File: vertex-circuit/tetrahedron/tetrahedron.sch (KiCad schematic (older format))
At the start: 9 parts, among them J1 DIP-BLACK-MALE-HEADER-VERT_4P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, J2 DIP-BLACK-MALE-HEADER-VERT_4P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, J3 DIP-BLACK-MALE-HEADER-VERT_4P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, J4 DIP-BLACK-MALE-HEADER-VERT_4P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, J5 JACK-DC-005, J6 DIP-BLACK-MALE-HEADER-VERT_4P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, J7 DIP-BLACK-MALE-HEADER-VERT_4P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, J8 DIP-BLACK-MALE-HEADER-VERT_4P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

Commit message: save circuits
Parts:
- removed J2, J3, J7, J8: DIP-BLACK-MALE-HEADER-VERT_4P-2.54_, SeeedOPL-Connector-2016:H4-2.54, symbol DIP-BLACK-MALE-HEADER-VERT_4P-2.54_
- added J5: d, SeeedOPL-Connector-2016:H4-2.54, symbol DIP-BLACK-MALE-HEADER-VERT_4P-2.54_
- J1: renamed from J5; value JACK-DC-005 -> DC 5v
- J2: renamed from J6; value DIP-BLACK-MALE-HEADER-VERT_4P-2.54_ -> a
- J3: renamed from J1; value DIP-BLACK-MALE-HEADER-VERT_4P-2.54_ -> b
- J4: value DIP-BLACK-MALE-HEADER-VERT_4P-2.54_ -> c
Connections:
- net GND: now reaches J2.1 (P$1), J3.1 (P$1)
- net GND: now also C1.2, J1.-1 (-), J4.1 (P$1), J5.1 (P$1)
- net +5V: now reaches J2.4 (P$4), J3.4 (P$4)
- net +5V: now also C1.1, J1.+, J4.4 (P$4), J5.4 (P$4)
- net at J4.2 (P$2): now also J5.2 (P$2)
- net at J4.3 (P$3): now also J5.3 (P$3)
- no-connect marks 19 -> 1
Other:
- moved on the sheet: C1, J1, J2, J3, J4

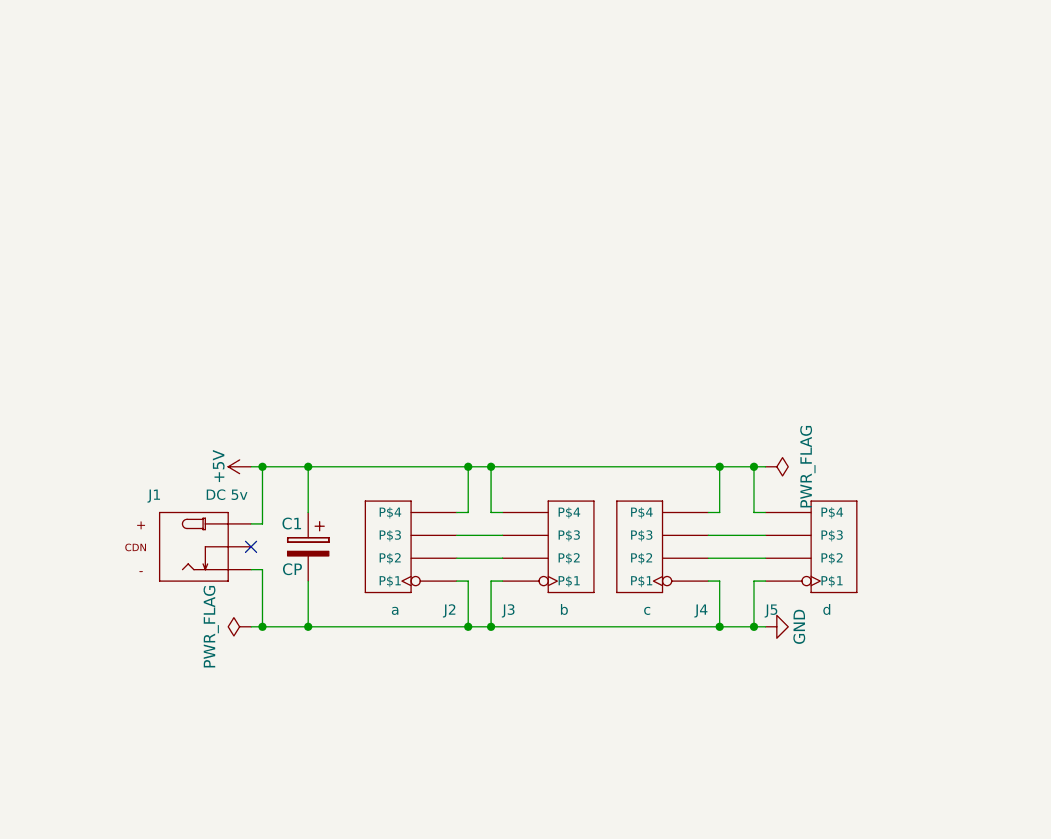
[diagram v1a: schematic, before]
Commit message: shematic electrical problems were only warnings! move on to pcb
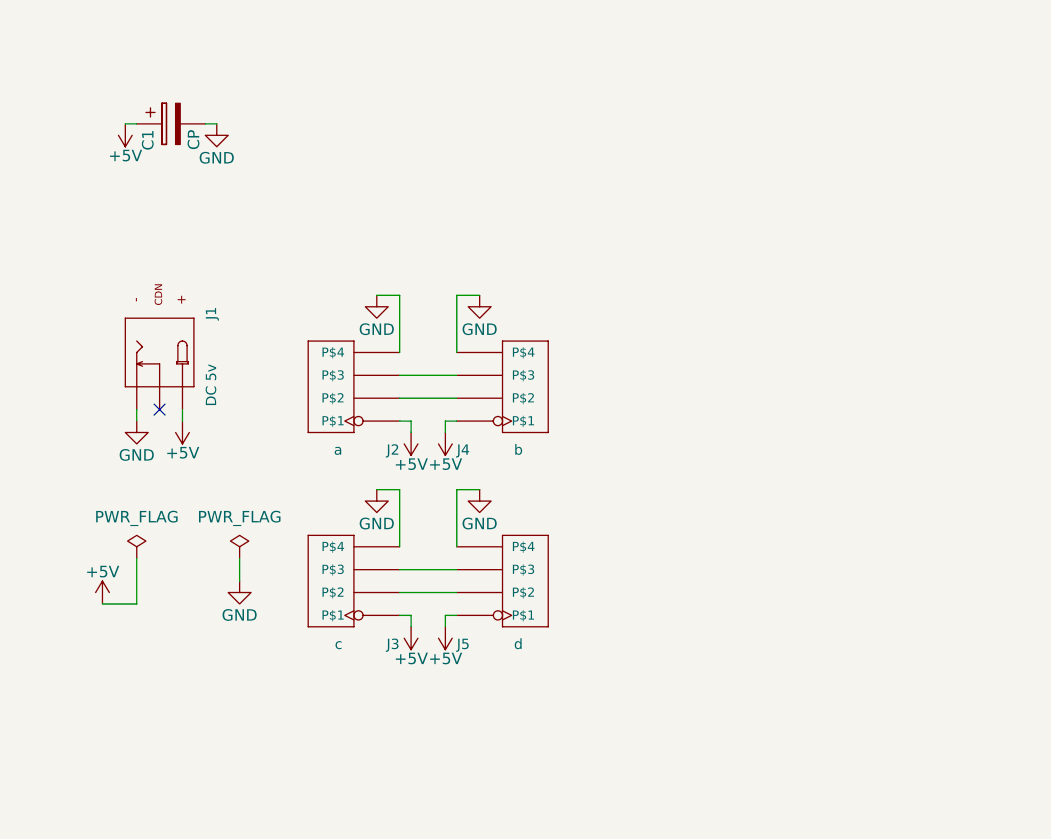
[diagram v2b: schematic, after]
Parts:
- removed J3: b, SeeedOPL-Connector-2016:H4-2.54, symbol DIP-BLACK-MALE-HEADER-VERT_4P-2.54_
- added J4: b, SeeedOPL-Connector-2016:H4-2.54, symbol DIP-BLACK-MALE-HEADER-VERT_4P-2.54_
- renumbered J4 to J3
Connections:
- net +5V: now also J2.1 (P$1), J3.1 (P$1), J5.1 (P$1), J4.1 (P$1); no longer J2.4 (P$4), J3.4 (P$4), J5.4 (P$4)
- net GND: now also J2.4 (P$4), J3.4 (P$4), J5.4 (P$4), J4.4 (P$4); no longer J2.1 (P$1), J3.1 (P$1), J5.1 (P$1)
- net at J2.2 (P$2): now also J4.2 (P$2)
- net at J2.3 (P$3): now also J4.3 (P$3)
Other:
- moved on the sheet: C1, J1, J3, J5

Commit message: circuity circuits
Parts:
- C1: footprint Discret:CP16 -> Capacitors_THT:CP_Radial_D10.0mm_P5.00mm
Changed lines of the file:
@@
 L GND #PWR02
 U 1 1 5B557715
-P 2000 2600
-F 0 "#PWR02" H 2000 2350 50  0001 C CNN
-F 1 "GND" H 2000 2450 50  0000 C CNN
-F 2 "" H 2000 2600 50  0000 C CNN
-F 3 "" H 2000 2600 50  0000 C CNN
-	1    2000 2600
+P 2100 2600
+F 0 "#PWR02" H 2100 2350 50  0001 C CNN
+F 1 "GND" H 2100 2450 50  0000 C CNN
+F 2 "" H 2100 2600 50  0000 C CNN
+F 3 "" H 2100 2600 50  0000 C CNN
+	1    2100 2600
 	1    0    0    -1
 $EndComp
@@
 L +5V #PWR03
 U 1 1 5B557A00
-P 2150 3200
-F 0 "#PWR03" H 2150 3050 50  0001 C CNN
-F 1 "+5V" H 2150 3340 50  0000 C CNN
-F 2 "" H 2150 3200 50  0000 C CNN
-F 3 "" H 2150 3200 50  0000 C CNN
-	1    2150 3200
-	-1   0    0    1
-$EndComp
-$Comp
-L +5V #PWR04
-U 1 1 5B557A6E
-P 2300 3200
-F 0 "#PWR04" H 2300 3050 50  0001 C CNN
-F 1 "+5V" H 2300 3340 50  0000 C CNN
-F 2 "" H 2300 3200 50  0000 C CNN
-F 3 "" H 2300 3200 50  0000 C CNN
-	1    2300 3200
-	-1   0    0    1
-$EndComp
-$Comp
-L GND #PWR05
-U 1 1 5B557A91
-P 2450 2600
-F 0 "#PWR05" H 2450 2350 50  0001 C CNN
-F 1 "GND" H 2450 2450 50  0000 C CNN
-F 2 "" H 2450 2600 50  0000 C CNN
-F 3 "" H 2450 2600 50  0000 C CNN
-	1    2450 2600
-	1    0    0    -1
+P 2250 3200
+F 0 "#PWR03" H 2250 3050 50  0001 C CNN
+F 1 "+5V" H 2250 3340 50  0000 C CNN
+F 2 "" H 2250 3200 50  0000 C CNN
+F 3 "" H 2250 3200 50  0000 C CNN
+	1    2250 3200
+	-1   0    0    1
 $EndComp
 $Comp
@@
 $EndComp
 $Comp
+L GND #PWR04
+U 1 1 5B557BFA
+P 2100 1750
+F 0 "#PWR04" H 2100 1500 50  0001 C CNN
+F 1 "GND" H 2100 1600 50  0000 C CNN
+F 2 "" H 2100 1750 50  0000 C CNN
+F 3 "" H 2100 1750 50  0000 C CNN
+	1    2100 1750
+	1    0    0    -1
+$EndComp
+$Comp
+L +5V #PWR05
+U 1 1 5B557C06
+P 2250 2350
+F 0 "#PWR05" H 2250 2200 50  0001 C CNN
+F 1 "+5V" H 2250 2490 50  0000 C CNN
+F 2 "" H 2250 2350 50  0000 C CNN
+F 3 "" H 2250 2350 50  0000 C CNN
+	1    2250 2350
+	-1   0    0    1
+$EndComp
+$Comp
 L GND #PWR06
-U 1 1 5B557BFA
-P 2000 1750
-F 0 "#PWR06" H 2000 1500 50  0001 C CNN
-F 1 "GND" H 2000 1600 50  0000 C CNN
-F 2 "" H 2000 1750 50  0000 C CNN
-F 3 "" H 2000 1750 50  0000 C CNN
-	1    2000 1750
-	1    0    0    -1
-$EndComp
-$Comp
-L +5V #PWR07
-U 1 1 5B557C00
-P 2150 2350
-F 0 "#PWR07" H 2150 2200 50  0001 C CNN
-F 1 "+5V" H 2150 2490 50  0000 C CNN
-F 2 "" H 2150 2350 50  0000 C CNN
-F 3 "" H 2150 2350 50  0000 C CNN
-	1    2150 2350
-	-1   0    0    1
-$EndComp
-$Comp
-L +5V #PWR08
-U 1 1 5B557C06
-P 2300 2350
-F 0 "#PWR08" H 2300 2200 50  0001 C CNN
-F 1 "+5V" H 2300 2490 50  0000 C CNN
-F 2 "" H 2300 2350 50  0000 C CNN
-F 3 "" H 2300 2350 50  0000 C CNN
-	1    2300 2350
-	-1   0    0    1
-$EndComp
-$Comp
-L GND #PWR09
-U 1 1 5B557C0C
-P 2450 1750
-F 0 "#PWR09" H 2450 1500 50  0001 C CNN
-F 1 "GND" H 2450 1600 50  0000 C CNN
-F 2 "" H 2450 1750 50  0000 C CNN
-F 3 "" H 2450 1750 50  0000 C CNN
-	1    2450 1750
-	1    0    0    -1
-$EndComp
-$Comp
-L GND #PWR010
 U 1 1 5B55813E
 P 1300 1000
-F 0 "#PWR010" H 1300 750 50  0001 C CNN
+F 0 "#PWR06" H 1300 750 50  0001 C CNN
 F 1 "GND" H 1300 850 50  0000 C CNN
 F 2 "" H 1300 1000 50  0000 C CNN
@@
 NoConn ~ 1050 2250
 $Comp
-L PWR_FLAG #FLG011
+L PWR_FLAG #FLG07
 U 1 1 5B558234
 P 950 2900
-F 0 "#FLG011" H 950 2995 50  0001 C CNN
+F 0 "#FLG07" H 950 2995 50  0001 C CNN
 F 1 "PWR_FLAG" H 950 3080 50  0000 C CNN
 F 2 "" H 950 2900 50  0000 C CNN
@@
 $EndComp
 $Comp
-L PWR_FLAG #FLG012
+L PWR_FLAG #FLG08
 U 1 1 5B55826C
 P 1400 2900
-F 0 "#FLG012" H 1400 2995 50  0001 C CNN
+F 0 "#FLG08" H 1400 2995 50  0001 C CNN
 F 1 "PWR_FLAG" H 1400 3080 50  0000 C CNN
 F 2 "" H 1400 2900 50  0000 C CNN
@@
 $EndComp
 $Comp
-L GND #PWR013
+L GND #PWR09
 U 1 1 5B55828C
 P 1400 3000
-F 0 "#PWR013" H 1400 2750 50  0001 C CNN
+F 0 "#PWR09" H 1400 2750 50  0001 C CNN
 F 1 "GND" H 1400 2850 50  0000 C CNN
 F 2 "" H 1400 3000 50  0000 C CNN
@@
 $EndComp
 $Comp
-L +5V #PWR014
+L +5V #PWR010
 U 1 1 5B5582AC
 P 800 3100
-F 0 "#PWR014" H 800 2950 50  0001 C CNN
+F 0 "#PWR010" H 800 2950 50  0001 C CNN
 F 1 "+5V" H 800 3240 50  0000 C CNN
 F 2 "" H 800 3100 50  0000 C CNN
@@
 F 0 "C1" H 1125 1100 50  0000 L CNN
 F 1 "CP" H 1125 900 50  0000 L CNN
-F 2 "Discret:CP16" H 1138 850 50  0001 C CNN
+F 2 "Capacitors_THT:CP_Radial_D10.0mm_P5.00mm" H 1138 850 50  0001 C CNN
 F 3 "" H 1100 1000 50  0000 C CNN
 	1    1100 1000
@@
 $EndComp
 $Comp
-L GND #PWR015
+L GND #PWR011
 U 1 1 5B5575DA
 P 950 2300
-F 0 "#PWR015" H 950 2050 50  0001 C CNN
+F 0 "#PWR011" H 950 2050 50  0001 C CNN
 F 1 "GND" H 950 2150 50  0000 C CNN
 F 2 "" H 950 2300 50  0000 C CNN
@@
 $EndComp
 $Comp
-L +5V #PWR016
+L +5V #PWR012
 U 1 1 5B5575FD
 P 1150 2300
-F 0 "#PWR016" H 1150 2150 50  0001 C CNN
+F 0 "#PWR012" H 1150 2150 50  0001 C CNN
 F 1 "+5V" H 1150 2440 50  0000 C CNN
 F 2 "" H 1150 2300 50  0000 C CNN
@@
 	-1   0    0    1
 $EndComp
-Wire Wire Line
-	2300 3150 2350 3150
-Wire Wire Line
-	2100 3150 2150 3150
+Connection ~ 2200 2850
+Wire Wire Line
+	2350 2850 2100 2850
+Connection ~ 2250 3150
+Wire Wire Line
+	2250 3150 2250 3200
+Connection ~ 2200 2000
+Connection ~ 2250 2300
+Wire Wire Line
+	2250 2350 2250 2300
+Wire Wire Line
+	2350 2000 2100 2000
+Wire Wire Line
+	1400 2900 1400 3000
+Wire Wire Line
+	950  3100 950  2900
+Wire Wire Line
+	800  3100 950  3100
+Wire Wire Line
+	1300 1000 1250 1000
+Wire Wire Line
+	950  1000 900  1000
+Wire Wire Line
+	2200 1750 2100 1750
+Wire Wire Line
+	2200 2000 2200 1750
+Wire Wire Line
+	1150 2250 1150 2300
+Wire Wire Line
+	950  2250 950  2300
+Wire Wire Line
+	2200 2600 2200 2850
+Wire Wire Line
+	2100 2600 2200 2600
+Wire Wire Line
+	2100 2100 2350 2100
+Wire Wire Line
+	2100 2200 2350 2200
+Wire Wire Line
+	2100 2300 2350 2300
+Wire Wire Line
+	2100 2950 2350 2950
 Wire Wire Line
 	2100 3050 2350 3050
 Wire Wire Line
-	2100 2950 2350 2950
-Wire Wire Line
-	2300 2300 2350 2300
-Wire Wire Line
-	2100 2300 2150 2300
-Wire Wire Line
-	2100 2200 2350 2200
-Wire Wire Line
-	2100 2100 2350 2100
-Wire Wire Line
-	2000 2600 2100 2600
-Wire Wire Line
-	2100 2600 2100 2850
-Wire Wire Line
-	2450 2600 2350 2600
-Wire Wire Line
-	2350 2600 2350 2850
-Wire Wire Line
-	2300 3150 2300 3200
-Wire Wire Line
-	2150 3150 2150 3200
-Wire Wire Line
-	950  2250 950  2300
-Wire Wire Line
-	1150 2250 1150 2300
-Wire Wire Line
-	2100 2000 2100 1750
-Wire Wire Line
-	2100 1750 2000 1750
-Wire Wire Line
-	2450 1750 2350 1750
-Wire Wire Line
-	2350 1750 2350 2000
-Wire Wire Line
-	2300 2300 2300 2350
-Wire Wire Line
-	2150 2300 2150 2350
-Wire Wire Line
-	950  1000 900  1000
-Wire Wire Line
-	1300 1000 1250 1000
-Wire Wire Line
-	800  3100 950  3100
-Wire Wire Line
-	950  3100 950  2900
-Wire Wire Line
-	1400 2900 1400 3000
+	2100 3150 2350 3150
 $EndSCHEMATC

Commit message: hey hey we can generate the entire circuit board meow!
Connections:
- net +5V: no longer J3.1 (P$1)
- no-connect marks 1 -> 2
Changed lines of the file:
@@
 Wire Wire Line
 	2350 2850 2100 2850
-Connection ~ 2250 3150
 Wire Wire Line
 	2250 3150 2250 3200
@@
 	2100 3050 2350 3050
 Wire Wire Line
-	2100 3150 2350 3150
+	2250 3150 2350 3150
+NoConn ~ 2100 3150
 $EndSCHEMATC
